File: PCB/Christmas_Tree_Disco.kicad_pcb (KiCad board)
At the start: 2 copper layers, 190.5 x 188.9 mm, 38 parts, among them U1 DEV_KIT_EK-TM4C123GXL, U2 TLC5955DCA

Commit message: Removed extra LED
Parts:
- removed FID1, FID2, FID3: Fiducial, local:Fiducial_Front_Layer
- moved C8 98.2 mm to (182.5, 97.4), turned to 270 degrees
- moved D8 96.3 mm to (183.1, 91.9), turned to 90 degrees
- moved C0 79.2 mm to (99.2, 63.2)
- moved D0 79.2 mm to (94.2, 66.7)
- moved D4 75.4 mm to (108.2, 111.5)
- moved C4 75.3 mm to (112.9, 108.4)
- moved C13 46.1 mm to (143.2, 102.2)
- moved D13 46.1 mm to (138.3, 105.6)
- moved C14 46.0 mm to (158.7, 140.3)
- moved D14 46.0 mm to (153.8, 143.8)
- moved C15 45.4 mm to (176.0, 182.8)
- moved D15 45.4 mm to (171.1, 186.3)
- moved C9 42.6 mm to (127.4, 63.1)
- moved D9 42.6 mm to (122.5, 66.5)
- moved C5 41.2 mm to (83.2, 101.9)
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
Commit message: Preliminary PCB layout
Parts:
- added C17: Capacitor-Pol, local:SMD-POL-1206, F.Cu at (102.7, 199.0)
- added C18: Capacitor, local:SMD-0805, F.Cu at (107.3, 164.2)
- added C19: Capacitor, local:SMD-0805, F.Cu at (111.0, 164.2)
- added F1: 24V 3A, local:SMD-2920, F.Cu at (116.8, 209.6)
- added H3: Snow Silk Screen, local:snow, B.Cu at (108.6, 124.0)
- added H301: 2x10 HEADER, local:2x10_header_3d, F.Cu at (87.5, 171.0)
- added H302: 2x10 HEADER, local:2x10_header_3d, F.Cu at (130.8, 171.0)
- added J1: PJ-006B-SMT-TR, local:PJ-006B-SMT, F.Cu at (130.8, 205.8)
- added U3: LM1085-5.0, local:TO-263, F.Cu at (94.2, 202.2)
- added U301: MC14504B, local:SOIC-16, F.Cu at (109.2, 172.7)
- added V1.0: www.github.com/Cryochasm, local:PCB-LABEL, F.Cu at (108.0, 101.6)
- C8: value Capacitor -> Capacitor-Pol; footprint local:SMD-0805 -> local:SMD-POL-1206
- D8: value RGB LED -> TVS-Bidirectional; footprint local:T-1_5mm -> local:DO-214AA
- moved D8 135.7 mm to (109.2, 205.7)
- moved C8 134.9 mm to (102.8, 206.2)
- moved C16 24.1 mm to (108.6, 116.9)
- moved U2 24.1 mm to (108.6, 127.0)
- moved U1 23.2 mm to (109.1, 170.9)
- moved C12 10.9 mm to (105.2, 35.8), turned to 270 degrees
- moved C14 10.3 mm to (148.8, 143.1), turned to 180 degrees
- moved C15 10.2 mm to (166.2, 185.4), turned to 180 degrees
- moved C9 10.2 mm to (117.6, 65.8), turned to 180 degrees
- moved C13 10.2 mm to (133.5, 105.1), turned to 180 degrees
- moved C7 3.24 mm to (113.2, 197.9)
- moved C5 3.10 mm to (83.0, 105.0)
- moved C3 2.95 mm to (81.3, 194.7)
- moved C2 2.86 mm to (97.8, 151.1)
- moved C10 2.79 mm to (128.9, 151.1)
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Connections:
- C0 pad 1: /Top Sheet/RGB LED Array/5V -> /Top Sheet/Microcontroller/5V
- C0 pad 2: /Top Sheet/RGB LED Array/GND -> /Top Sheet/Microcontroller/GND
- C1 pad 1: /Top Sheet/RGB LED Array/5V -> /Top Sheet/Microcontroller/5V
- C1 pad 2: /Top Sheet/RGB LED Array/GND -> /Top Sheet/Microcontroller/GND
- C10 pad 1: /Top Sheet/RGB LED Array/5V -> /Top Sheet/Microcontroller/5V
- C10 pad 2: /Top Sheet/RGB LED Array/GND -> /Top Sheet/Microcontroller/GND
- C11 pad 1: /Top Sheet/RGB LED Array/5V -> /Top Sheet/Microcontroller/5V
- C11 pad 2: /Top Sheet/RGB LED Array/GND -> /Top Sheet/Microcontroller/GND
- C12 pad 1: /Top Sheet/RGB LED Array/5V -> /Top Sheet/Microcontroller/5V
- C12 pad 2: /Top Sheet/RGB LED Array/GND -> /Top Sheet/Microcontroller/GND
- C13 pad 1: /Top Sheet/RGB LED Array/5V -> /Top Sheet/Microcontroller/5V
- C13 pad 2: /Top Sheet/RGB LED Array/GND -> /Top Sheet/Microcontroller/GND
- C14 pad 1: /Top Sheet/RGB LED Array/5V -> /Top Sheet/Microcontroller/5V
- C14 pad 2: /Top Sheet/RGB LED Array/GND -> /Top Sheet/Microcontroller/GND
- C15 pad 1: /Top Sheet/RGB LED Array/5V -> /Top Sheet/Microcontroller/5V
- C15 pad 2: /Top Sheet/RGB LED Array/GND -> /Top Sheet/Microcontroller/GND
- C16 pad 1: /Top Sheet/RGB LED Array/GND -> /Top Sheet/Microcontroller/GND
- C16 pad 2: /Top Sheet/RGB LED Array/5V -> /Top Sheet/Microcontroller/5V
- C2 pad 1: /Top Sheet/RGB LED Array/5V -> /Top Sheet/Microcontroller/5V
- C2 pad 2: /Top Sheet/RGB LED Array/GND -> /Top Sheet/Microcontroller/GND
- C3 pad 1: /Top Sheet/RGB LED Array/5V -> /Top Sheet/Microcontroller/5V
- C3 pad 2: /Top Sheet/RGB LED Array/GND -> /Top Sheet/Microcontroller/GND
- C4 pad 1: /Top Sheet/RGB LED Array/5V -> /Top Sheet/Microcontroller/5V
- C4 pad 2: /Top Sheet/RGB LED Array/GND -> /Top Sheet/Microcontroller/GND
- C5 pad 1: /Top Sheet/RGB LED Array/5V -> /Top Sheet/Microcontroller/5V
- C5 pad 2: /Top Sheet/RGB LED Array/GND -> /Top Sheet/Microcontroller/GND
- C6 pad 1: /Top Sheet/RGB LED Array/5V -> /Top Sheet/Microcontroller/5V
- C6 pad 2: /Top Sheet/RGB LED Array/GND -> /Top Sheet/Microcontroller/GND
- C7 pad 1: /Top Sheet/RGB LED Array/5V -> /Top Sheet/Microcontroller/5V
- C7 pad 2: /Top Sheet/RGB LED Array/GND -> /Top Sheet/Microcontroller/GND
- C8 pad 1: /Top Sheet/RGB LED Array/5V -> /Top Sheet/Microcontroller/GND
- C8 pad 2: /Top Sheet/RGB LED Array/GND -> Net-(C8-Pad2)
- C9 pad 1: /Top Sheet/RGB LED Array/5V -> /Top Sheet/Microcontroller/5V
- C9 pad 2: /Top Sheet/RGB LED Array/GND -> /Top Sheet/Microcontroller/GND
- D0 pad 2: /Top Sheet/RGB LED Array/5V -> /Top Sheet/Microcontroller/5V
- D1 pad 2: /Top Sheet/RGB LED Array/5V -> /Top Sheet/Microcontroller/5V
- D10 pad 2: /Top Sheet/RGB LED Array/5V -> /Top Sheet/Microcontroller/5V
- D11 pad 2: /Top Sheet/RGB LED Array/5V -> /Top Sheet/Microcontroller/5V
- D12 pad 2: /Top Sheet/RGB LED Array/5V -> /Top Sheet/Microcontroller/5V
- D13 pad 2: /Top Sheet/RGB LED Array/5V -> /Top Sheet/Microcontroller/5V
- D14 pad 2: /Top Sheet/RGB LED Array/5V -> /Top Sheet/Microcontroller/5V
- D15 pad 2: /Top Sheet/RGB LED Array/5V -> /Top Sheet/Microcontroller/5V
- D2 pad 2: /Top Sheet/RGB LED Array/5V -> /Top Sheet/Microcontroller/5V
- D3 pad 2: /Top Sheet/RGB LED Array/5V -> /Top Sheet/Microcontroller/5V
- D4 pad 2: /Top Sheet/RGB LED Array/5V -> /Top Sheet/Microcontroller/5V
- D5 pad 2: /Top Sheet/RGB LED Array/5V -> /Top Sheet/Microcontroller/5V
- D6 pad 2: /Top Sheet/RGB LED Array/5V -> /Top Sheet/Microcontroller/5V
- D7 pad 2: /Top Sheet/RGB LED Array/5V -> /Top Sheet/Microcontroller/5V
- D8 pad 1: /Top Sheet/RGB LED Array/RGB08_1 -> Net-(C8-Pad2)
- D8 pad 2: /Top Sheet/RGB LED Array/5V -> /Top Sheet/Microcontroller/GND
- D9 pad 2: /Top Sheet/RGB LED Array/5V -> /Top Sheet/Microcontroller/5V
- U1 pad 1: Net-(U1-Pad1) -> /Top Sheet/Microcontroller/3V3
- U2 pad 1: /Top Sheet/RGB LED Array/DATA -> /Top Sheet/Microcontroller/DATA
- U2 pad 2: /Top Sheet/RGB LED Array/SCLK -> /Top Sheet/Microcontroller/SCLK
- U2 pad 28: /Top Sheet/RGB LED Array/ERROR_RD -> /Top Sheet/Microcontroller/ERROR_RD
- U2 pad 29: /Top Sheet/RGB LED Array/GND -> /Top Sheet/Microcontroller/GND
- U2 pad 3: /Top Sheet/RGB LED Array/LAT -> /Top Sheet/Microcontroller/LAT
- U2 pad 51: /Top Sheet/RGB LED Array/RGB08_2 -> Net-(U2-Pad51)
- U2 pad 52: /Top Sheet/RGB LED Array/RGB08_1 -> Net-(U2-Pad52)
- U2 pad 53: /Top Sheet/RGB LED Array/RGB08_0 -> Net-(U2-Pad53)
- U2 pad 54: /Top Sheet/RGB LED Array/5V -> /Top Sheet/Microcontroller/5V
- U2 pad 55: /Top Sheet/RGB LED Array/GSCLK -> /Top Sheet/Microcontroller/GSCLK
- U2 pad 56: /Top Sheet/RGB LED Array/GND -> /Top Sheet/Microcontroller/GND
- U2 pad EP: /Top Sheet/RGB LED Array/GND -> /Top Sheet/Microcontroller/GND
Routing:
- added copper zone on B.Cu, net /Top Sheet/Microcontroller/GND
- added copper zone on F.Cu, net /Top Sheet/Microcontroller/GND
- added copper zone on F.Cu, net /Top Sheet/Power Supply/VIN
- added copper zone on F.Cu, net Net-(C8-Pad2)
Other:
- net class Default: clearance 0 -> 0.15; via_dia 0.8 -> 0.686; via_drill 0.4 -> 0.432
- rule trace_clearance: 0 -> 0.15
- board text removed: "12.5000"

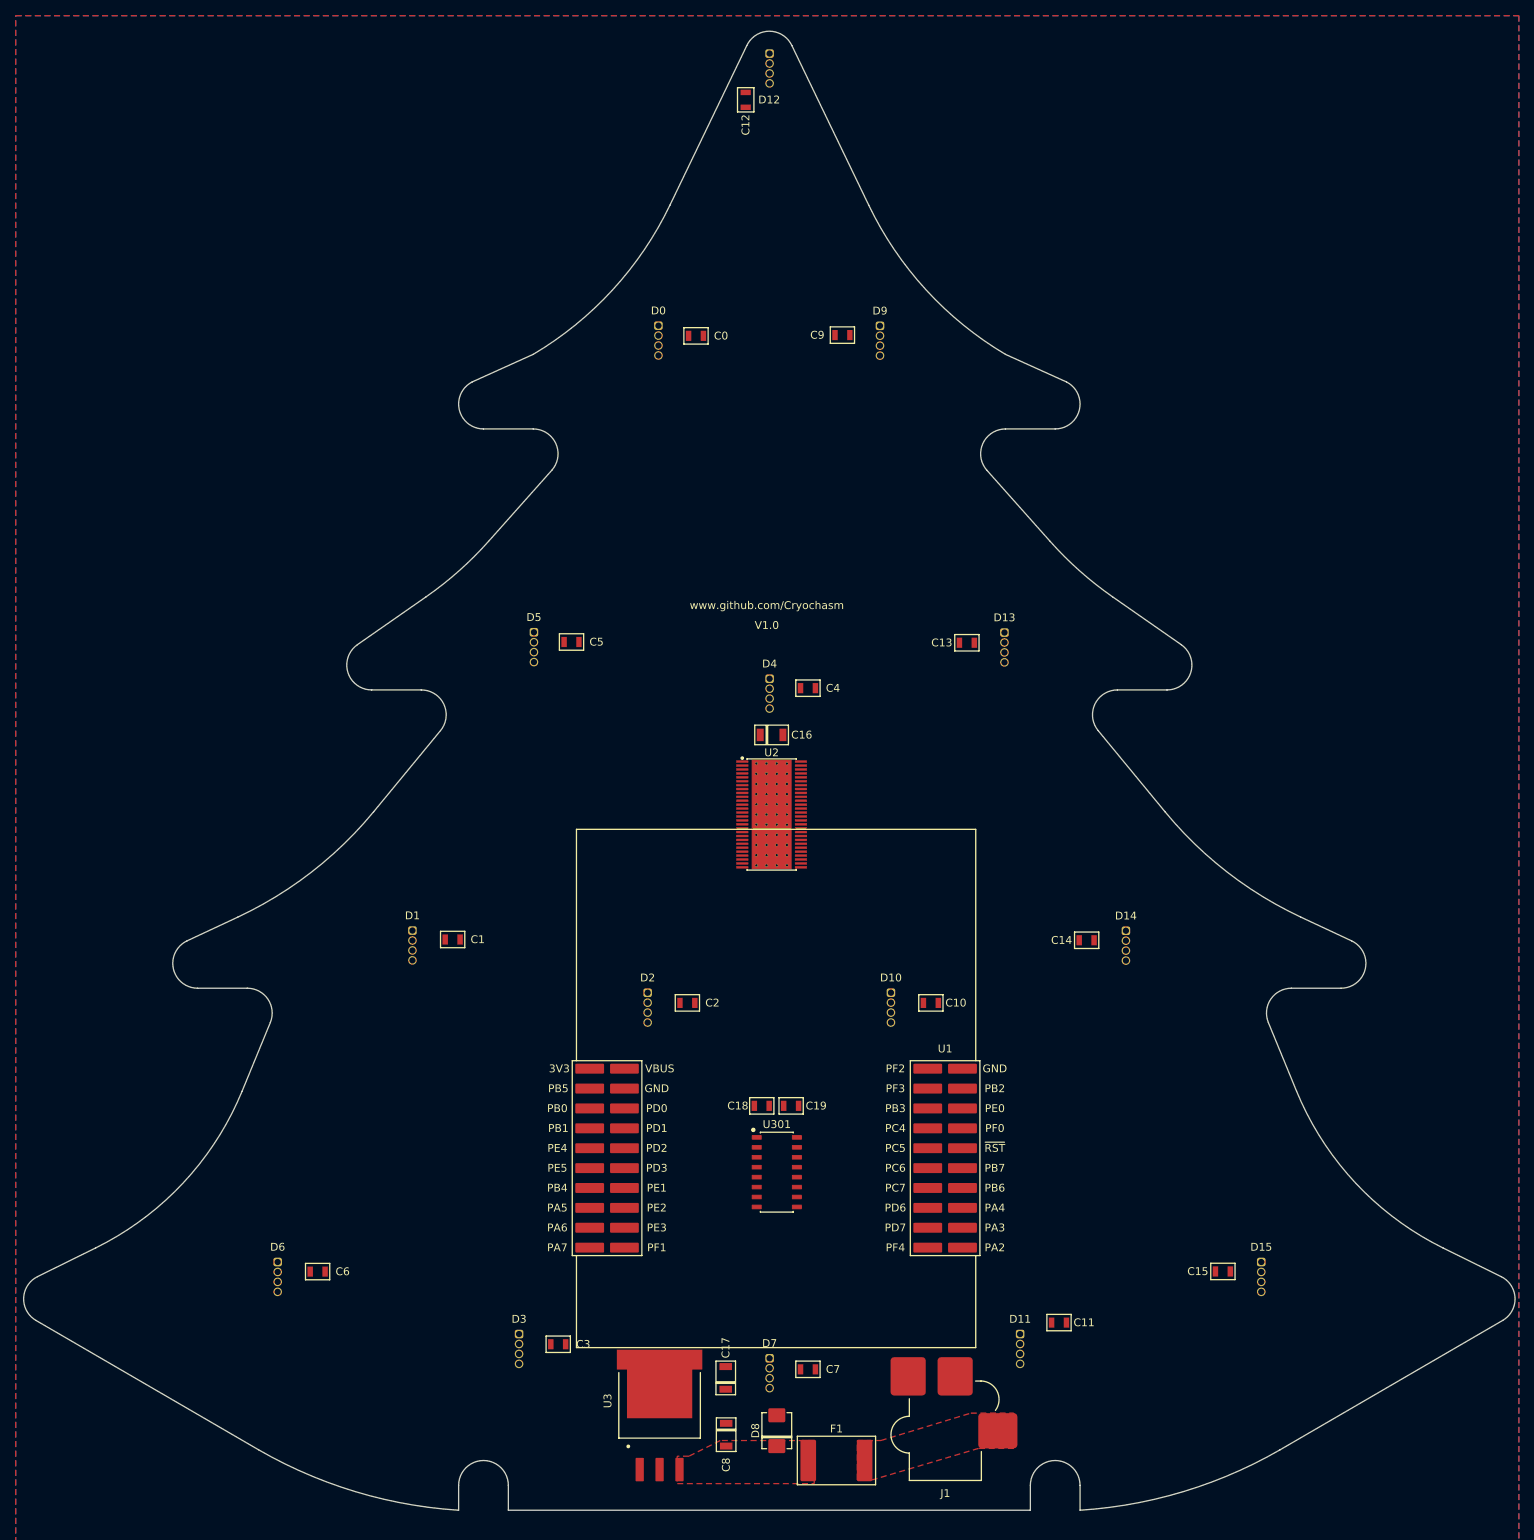
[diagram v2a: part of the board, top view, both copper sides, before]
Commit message: PCB Layout
TODO: Change pinouts on dev kit to be compatable with Capacitive Touch
Audio booster pack.
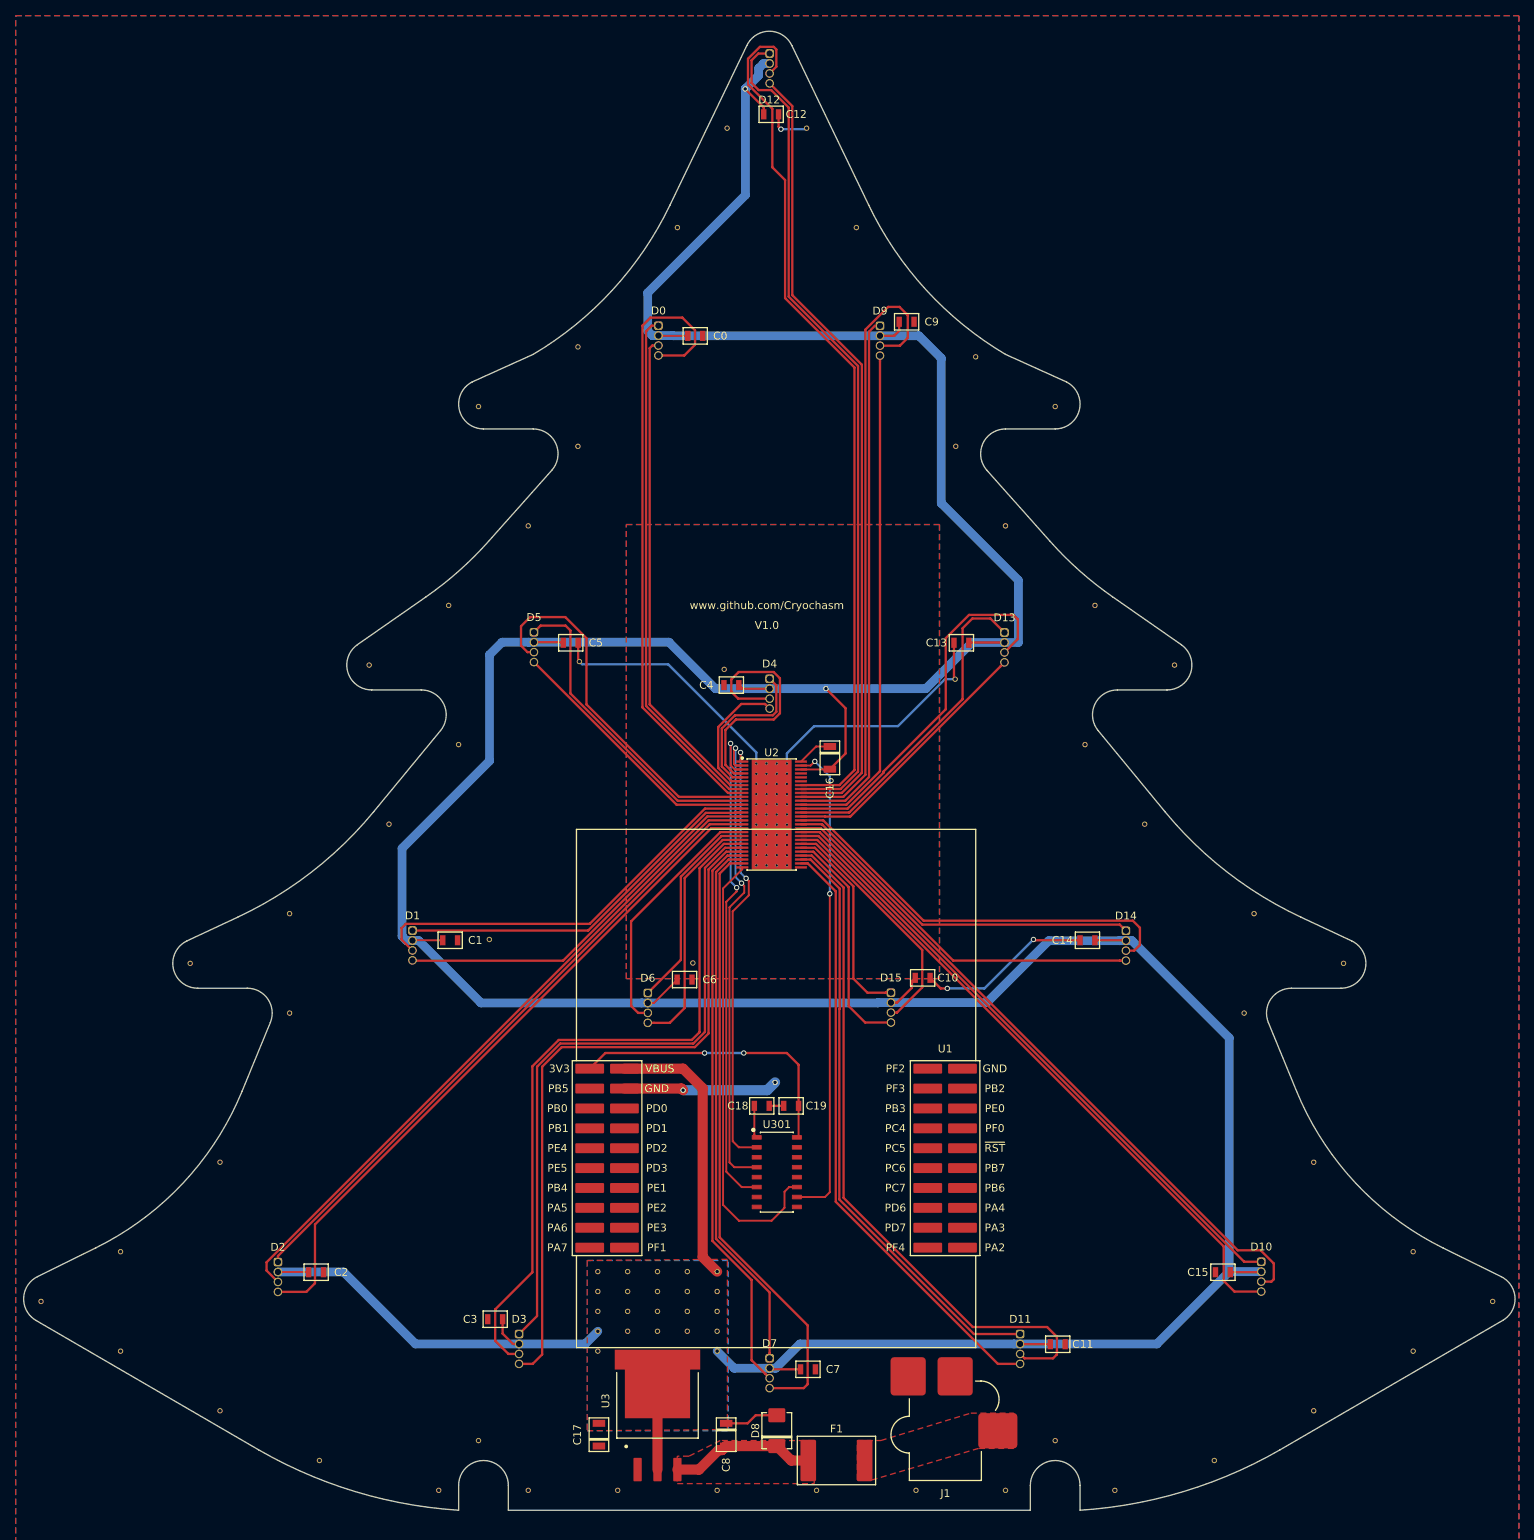
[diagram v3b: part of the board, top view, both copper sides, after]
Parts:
- removed the C1 at (67.8, 143.0)
- added C9: 0.1u, local:SMD-0805, F.Cu at (125.8, 64.1)
- added STITCH: VIA-432-686, local:VIA-432-686, F.Cu at (132.0, 109.8)
- added STITCH: VIA-432-686, local:VIA-432-686, F.Cu at (114.3, 213.4)
- added STITCH: VIA-432-686, local:VIA-432-686, F.Cu at (127.0, 213.4)
- added STITCH: VIA-432-686, local:VIA-432-686, F.Cu at (138.4, 213.4)
- added STITCH: VIA-432-686, local:VIA-432-686, F.Cu at (144.8, 207.0)
- added STITCH: VIA-432-686, local:VIA-432-686, F.Cu at (152.4, 213.4)
- added STITCH: VIA-432-686, local:VIA-432-686, F.Cu at (165.1, 209.6)
- added STITCH: VIA-432-686, local:VIA-432-686, F.Cu at (177.8, 203.2)
- added STITCH: VIA-432-686, local:VIA-432-686, F.Cu at (190.5, 195.6)
- added STITCH: VIA-432-686, local:VIA-432-686, F.Cu at (200.7, 189.2)
- added STITCH: VIA-432-686, local:VIA-432-686, F.Cu at (190.5, 182.9)
- added STITCH: VIA-432-686, local:VIA-432-686, F.Cu at (102.5, 108.5)
- added STITCH: VIA-432-686, local:VIA-432-686, F.Cu at (177.8, 171.4)
- added STITCH: VIA-432-686, local:VIA-432-686, F.Cu at (168.9, 152.4)
- added STITCH: VIA-432-686, local:VIA-432-686, F.Cu at (181.6, 146.1)
- added STITCH: VIA-432-686, local:VIA-432-686, F.Cu at (170.2, 139.7)
- added STITCH: VIA-432-686, local:VIA-432-686, F.Cu at (156.2, 128.3)
- added STITCH: VIA-432-686, local:VIA-432-686, F.Cu at (148.6, 118.1)
- added STITCH: VIA-432-686, local:VIA-432-686, F.Cu at (160.0, 108.0)
- added STITCH: VIA-432-686, local:VIA-432-686, F.Cu at (149.9, 100.3)
- added STITCH: VIA-432-686, local:VIA-432-686, F.Cu at (138.4, 90.2)
- added STITCH: VIA-432-686, local:VIA-432-686, F.Cu at (132.1, 80.0)
- added STITCH: VIA-432-686, local:VIA-432-686, F.Cu at (84.0, 107.5)
- added STITCH: VIA-432-686, local:VIA-432-686, F.Cu at (144.8, 74.9)
- added STITCH: VIA-432-686, local:VIA-432-686, F.Cu at (134.6, 68.6)
- added STITCH: VIA-432-686, local:VIA-432-686, F.Cu at (119.4, 52.1)
- added STITCH: VIA-432-686, local:VIA-432-686, F.Cu at (113.0, 39.4)
- added STITCH: VIA-432-686, local:VIA-432-686, F.Cu at (102.9, 39.4)
- added STITCH: VIA-432-686, local:VIA-432-686, F.Cu at (96.5, 52.1)
- added STITCH: VIA-432-686, local:VIA-432-686, F.Cu at (83.8, 67.3)
- added STITCH: VIA-432-686, local:VIA-432-686, F.Cu at (71.1, 74.9)
- added STITCH: VIA-432-686, local:VIA-432-686, F.Cu at (83.8, 80.0)
- added STITCH: VIA-432-686, local:VIA-432-686, F.Cu at (77.5, 90.2)
- added STITCH: VIA-432-686, local:VIA-432-686, F.Cu at (72.5, 143.0)
- added STITCH: VIA-432-686, local:VIA-432-686, F.Cu at (67.3, 100.3)
- added STITCH: VIA-432-686, local:VIA-432-686, F.Cu at (57.1, 108.0)
- added STITCH: VIA-432-686, local:VIA-432-686, F.Cu at (68.6, 118.1)
- added STITCH: VIA-432-686, local:VIA-432-686, F.Cu at (59.7, 128.3)
- added STITCH: VIA-432-686, local:VIA-432-686, F.Cu at (47.0, 139.7)
- added STITCH: VIA-432-686, local:VIA-432-686, F.Cu at (34.3, 146.1)
- added STITCH: VIA-432-686, local:VIA-432-686, F.Cu at (47.0, 152.4)
- added STITCH: VIA-432-686, local:VIA-432-686, F.Cu at (38.1, 171.4)
- added STITCH: VIA-432-686, local:VIA-432-686, F.Cu at (25.4, 182.9)
- added STITCH: VIA-432-686, local:VIA-432-686, F.Cu at (15.2, 189.2)
- added STITCH: VIA-432-686, local:VIA-432-686, F.Cu at (98.5, 146.0)
- added STITCH: VIA-432-686, local:VIA-432-686, F.Cu at (25.4, 195.6)
- added STITCH: VIA-432-686, local:VIA-432-686, F.Cu at (38.1, 203.2)
- added STITCH: VIA-432-686, local:VIA-432-686, F.Cu at (50.8, 209.6)
- added STITCH: VIA-432-686, local:VIA-432-686, F.Cu at (101.6, 195.6)
- added STITCH: VIA-432-686, local:VIA-432-686, F.Cu at (86.4, 195.6)
- added STITCH: VIA-432-686, local:VIA-432-686, F.Cu at (86.4, 185.4)
- added STITCH: VIA-432-686, local:VIA-432-686, F.Cu at (86.4, 188.0)
- added STITCH: VIA-432-686, local:VIA-432-686, F.Cu at (94.0, 185.4)
- added STITCH: VIA-432-686, local:VIA-432-686, F.Cu at (97.8, 185.4)
- added STITCH: VIA-432-686, local:VIA-432-686, F.Cu at (101.6, 185.4)
- added STITCH: VIA-432-686, local:VIA-432-686, F.Cu at (71.1, 207.0)
- added STITCH: VIA-432-686, local:VIA-432-686, F.Cu at (101.6, 188.0)
- added STITCH: VIA-432-686, local:VIA-432-686, F.Cu at (86.4, 190.5)
- added STITCH: VIA-432-686, local:VIA-432-686, F.Cu at (101.6, 190.5)
- added STITCH: VIA-432-686, local:VIA-432-686, F.Cu at (97.8, 190.5)
- added STITCH: VIA-432-686, local:VIA-432-686, F.Cu at (90.2, 190.5)
- added STITCH: VIA-432-686, local:VIA-432-686, F.Cu at (94.0, 188.0)
- added STITCH: VIA-432-686, local:VIA-432-686, F.Cu at (94.0, 190.5)
- added STITCH: VIA-432-686, local:VIA-432-686, F.Cu at (97.8, 188.0)
- added STITCH: VIA-432-686, local:VIA-432-686, F.Cu at (90.2, 188.0)
- added STITCH: VIA-432-686, local:VIA-432-686, F.Cu at (94.0, 193.0)
- added STITCH: VIA-432-686, local:VIA-432-686, F.Cu at (77.5, 213.4)
- added STITCH: VIA-432-686, local:VIA-432-686, F.Cu at (90.2, 185.4)
- added STITCH: VIA-432-686, local:VIA-432-686, F.Cu at (101.6, 193.0)
- added STITCH: VIA-432-686, local:VIA-432-686, F.Cu at (97.8, 193.0)
- added STITCH: VIA-432-686, local:VIA-432-686, F.Cu at (90.2, 193.0)
- added STITCH: VIA-432-686, local:VIA-432-686, F.Cu at (86.4, 193.0)
- added STITCH: VIA-432-686, local:VIA-432-686, F.Cu at (66.0, 213.4)
- added STITCH: VIA-432-686, local:VIA-432-686, F.Cu at (88.9, 213.4)
- added STITCH: VIA-432-686, local:VIA-432-686, F.Cu at (101.6, 213.4)
- C0, C10, C11, C12, C13, C14, C15, C18, C19, C3, C5, C6, C7: value Capacitor -> 0.1u
- C1: renamed from C9; value Capacitor -> 0.1u
- C16, C17, C8: value Capacitor-Pol -> 10u
- C2: renamed from C4; value Capacitor -> 0.1u
- C4: renamed from C2; value Capacitor -> 0.1u
- D8: value TVS-Bidirectional -> SMBJ22D-M3/H
- moved C2 97.5 mm to (50.4, 185.5)
- moved C1 92.1 mm to (67.5, 143.1), turned to 0 degrees
- moved C6 59.9 mm to (97.4, 148.1)
- moved D15 58.5 mm to (123.8, 151.7)
- moved D10 58.5 mm to (171.1, 186.1)
- moved D6 58.4 mm to (92.7, 151.7)
- moved D2 58.4 mm to (45.5, 186.1)
- moved C4 41.0 mm to (103.4, 110.5), turned to 180 degrees
- moved C17 17.7 mm to (86.5, 206.2)
- moved C3 8.66 mm to (73.2, 191.5), turned to 180 degrees
- moved C16 8.00 mm to (116.0, 119.8), turned to 270 degrees
- moved C12 3.74 mm to (108.5, 37.6), turned to 0 degrees
- moved C10 3.37 mm to (127.8, 147.9)
- moved C11 2.77 mm to (145.1, 194.7)
- moved C13 0.70 mm to (132.8, 105.1)
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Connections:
- net Net-(C8-Pad2) renamed /Top Sheet/Power Supply/VIN_FUSED
- net Net-(U1-Pad27) renamed /Top Sheet/Microcontroller/LAT_3V3
- net Net-(U1-Pad28) renamed /Top Sheet/Microcontroller/SCLK_3V3
- net Net-(U1-Pad29) renamed /Top Sheet/Microcontroller/DATA_3V3
- net Net-(U1-Pad30) renamed /Top Sheet/Microcontroller/GSCLK_3V3
- net Net-(U1-Pad31) renamed /Top Sheet/Microcontroller/ERROR_RD_3V3
- J1 pad 3: Net-(J1-Pad3) -> (no net)
- U1 pad 10: Net-(U1-Pad10) -> (no net)
- U1 pad 11: Net-(U1-Pad11) -> (no net)
- U1 pad 12: Net-(U1-Pad12) -> (no net)
- U1 pad 13: Net-(U1-Pad13) -> (no net)
- U1 pad 14: Net-(U1-Pad14) -> (no net)
- U1 pad 15: Net-(U1-Pad15) -> (no net)
- U1 pad 16: Net-(U1-Pad16) -> (no net)
- U1 pad 17: Net-(U1-Pad17) -> (no net)
- U1 pad 18: Net-(U1-Pad18) -> (no net)
- U1 pad 2: Net-(U1-Pad2) -> (no net)
- U1 pad 21: Net-(U1-Pad21) -> (no net)
- U1 pad 22: Net-(U1-Pad22) -> (no net)
- U1 pad 23: Net-(U1-Pad23) -> (no net)
- U1 pad 24: Net-(U1-Pad24) -> (no net)
- U1 pad 25: Net-(U1-Pad25) -> (no net)
- U1 pad 26: Net-(U1-Pad26) -> (no net)
- U1 pad 3: Net-(U1-Pad3) -> (no net)
- U1 pad 32: Net-(U1-Pad32) -> (no net)
- U1 pad 33: Net-(U1-Pad33) -> (no net)
- U1 pad 34: Net-(U1-Pad34) -> (no net)
- U1 pad 35: Net-(U1-Pad35) -> (no net)
- U1 pad 36: Net-(U1-Pad36) -> (no net)
- U1 pad 37: Net-(U1-Pad37) -> (no net)
- U1 pad 38: Net-(U1-Pad38) -> (no net)
- U1 pad 39: Net-(U1-Pad39) -> (no net)
- U1 pad 4: Net-(U1-Pad4) -> (no net)
- U1 pad 5: Net-(U1-Pad5) -> (no net)
- U1 pad 6: Net-(U1-Pad6) -> (no net)
- U1 pad 7: Net-(U1-Pad7) -> (no net)
- U1 pad 8: Net-(U1-Pad8) -> (no net)
- U1 pad 9: Net-(U1-Pad9) -> (no net)
- U2 pad 51: Net-(U2-Pad51) -> (no net)
- U2 pad 52: Net-(U2-Pad52) -> (no net)
- U2 pad 53: Net-(U2-Pad53) -> (no net)
- U301 pad 14: Net-(U301-Pad14) -> (no net)
- U301 pad 15: Net-(U301-Pad15) -> (no net)
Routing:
- net /Top Sheet/Microcontroller/5V: track 0.00 -> 629.8 mm, vias 0 -> 2
- net /Top Sheet/Microcontroller/GND: track 0.00 -> 123.4 mm, vias 0 -> 5
- net /Top Sheet/RGB LED Array/RGB12_0: track 0.00 -> 111.9 mm
- net /Top Sheet/RGB LED Array/RGB12_1: track 0.00 -> 108.3 mm
- net /Top Sheet/RGB LED Array/RGB12_2: track 0.00 -> 101.8 mm
- net /Top Sheet/RGB LED Array/RGB03_0: track 0.00 -> 91.6 mm
- net /Top Sheet/RGB LED Array/RGB03_2: track 0.00 -> 89.4 mm
- net /Top Sheet/RGB LED Array/RGB11_0: track 0.00 -> 88.8 mm
- net /Top Sheet/RGB LED Array/RGB02_2: track 0.00 -> 88.2 mm
- net /Top Sheet/RGB LED Array/RGB02_0: track 0.00 -> 87.2 mm
- net /Top Sheet/RGB LED Array/RGB10_0: track 0.00 -> 87.0 mm
- net /Top Sheet/RGB LED Array/RGB10_2: track 0.00 -> 85.3 mm
- net /Top Sheet/RGB LED Array/RGB03_1: track 0.00 -> 85.2 mm
- net /Top Sheet/RGB LED Array/RGB02_1: track 0.00 -> 82.9 mm
- net /Top Sheet/RGB LED Array/RGB10_1: track 0.00 -> 81.3 mm
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- added copper zone on B.Cu, net /Top Sheet/Microcontroller/5V
- added copper zone on F.Cu, net /Top Sheet/Microcontroller/5V
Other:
- net class Comunications added: clearance 0.16, trace_width 0.25, via_dia 0.686, via_drill 0.432
- net class Default: clearance 0.15 -> 0.16
- net class LED_Sink added: clearance 0.16, trace_width 0.3, via_dia 0.686, via_drill 0.432
- rule trace_clearance: 0.15 -> 0.16
